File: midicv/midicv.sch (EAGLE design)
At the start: 33 parts, among them IC1 OPA2134P, J1 UBBS-4R-D14-4D, X1 2516-

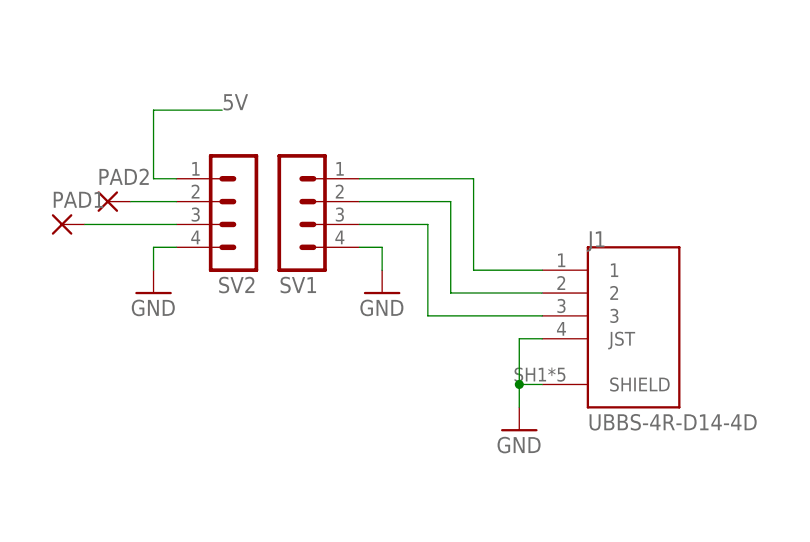
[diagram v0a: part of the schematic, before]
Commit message: fixed usb polatiry on midicv.  moved holes
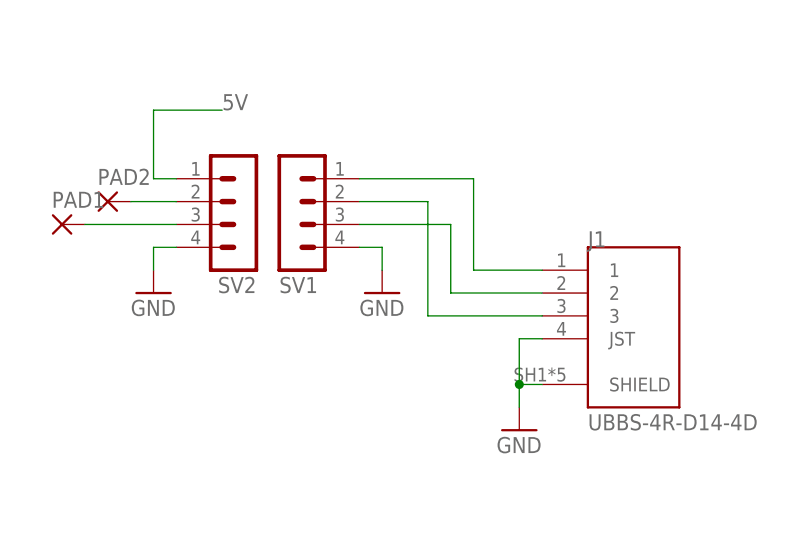
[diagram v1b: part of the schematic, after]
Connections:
- removed net N$9: J1.2, SV1.2
- new net N$18: J1.2, SV1.3
- net N$11: now also SV1.2; no longer SV1.3
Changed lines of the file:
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@@
-</segment>
-</net>
-<net name="N$9" class="0">
-<segment>
-<pinref part="SV1" gate="1" pin="2"/>
-<wire x1="175.26" y1="177.8" x2="185.42" y2="177.8" width="0.1524" layer="91"/>
-<wire x1="185.42" y1="177.8" x2="185.42" y2="167.64" width="0.1524" layer="91"/>
-<pinref part="J1" gate="G$1" pin="2"/>
-<wire x1="185.42" y1="167.64" x2="195.58" y2="167.64" width="0.1524" layer="91"/>
 </segment>
 </net>
@@
 <pinref part="J1" gate="G$1" pin="3"/>
 <wire x1="195.58" y1="165.1" x2="182.88" y2="165.1" width="0.1524" layer="91"/>
-<wire x1="182.88" y1="165.1" x2="182.88" y2="175.26" width="0.1524" layer="91"/>
-<pinref part="SV1" gate="1" pin="3"/>
-<wire x1="182.88" y1="175.26" x2="175.26" y2="175.26" width="0.1524" layer="91"/>
+<pinref part="SV1" gate="1" pin="2"/>
+<wire x1="175.26" y1="177.8" x2="182.88" y2="177.8" width="0.1524" layer="91"/>
+<wire x1="182.88" y1="177.8" x2="182.88" y2="165.1" width="0.1524" layer="91"/>
 </segment>
 </net>
@@
 </segment>
 </net>
+<net name="N$18" class="0">
+<segment>
+<pinref part="SV1" gate="1" pin="3"/>
+<wire x1="185.42" y1="175.26" x2="175.26" y2="175.26" width="0.1524" layer="91"/>
+<pinref part="J1" gate="G$1" pin="2"/>
+<wire x1="185.42" y1="167.64" x2="195.58" y2="167.64" width="0.1524" layer="91"/>
+<wire x1="185.42" y1="175.26" x2="185.42" y2="167.64" width="0.1524" layer="91"/>
+</segment>
+</net>
